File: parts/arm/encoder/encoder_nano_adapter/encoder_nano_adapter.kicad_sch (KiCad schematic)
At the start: 4 parts, among them J1 AS5600_power, J2 AS5600_I2C, J3 Servo

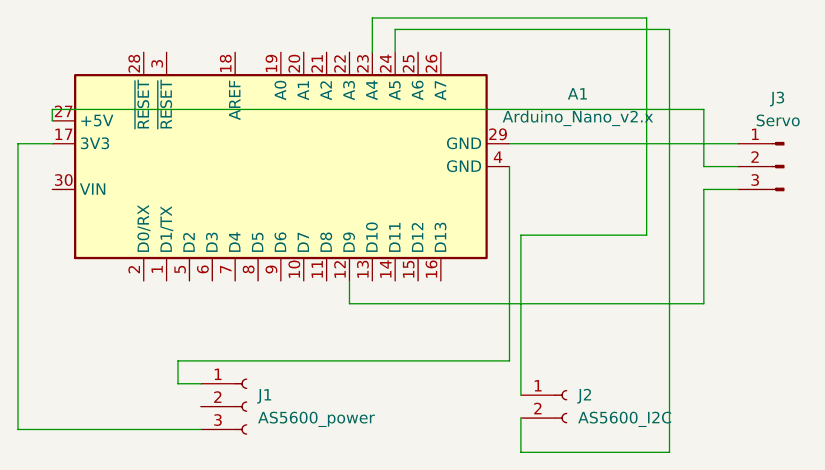
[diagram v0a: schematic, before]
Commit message: Stretch the wiretube so you can feed a USB or Anderson through while assembled.  Also added mounting screw to nano adapter board.
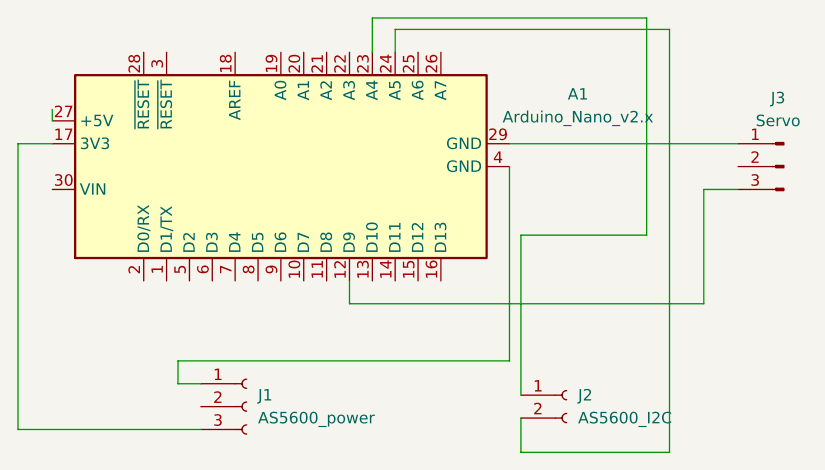
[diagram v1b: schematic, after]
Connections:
- net at J3.2 (Pin_2): no longer A1.27 (+5V)
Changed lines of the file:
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@@
-	(wire
-		(pts
-			(xy 116.84 20.32) (xy 116.84 26.67)
-		)
-		(stroke
-			(width 0)
-			(type default)
-		)
-	)
 	(wire
 		(pts
@@
 	(wire
 		(pts
-			(xy 44.45 20.32) (xy 116.84 20.32)
-		)
-		(stroke
-			(width 0)
-			(type default)
-		)
-	)
-	(wire
-		(pts
 			(xy 96.52 34.29) (xy 110.49 34.29)
 		)
@@
 		)
 		(stroke
-			(width 0)
-			(type default)
-		)
-	)
-	(wire
-		(pts
-			(xy 116.84 26.67) (xy 120.65 26.67)
-		)
-		(stroke
